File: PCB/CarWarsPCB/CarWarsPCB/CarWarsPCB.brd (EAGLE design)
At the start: 57.1 x 50.5 mm, 11 parts, among them J1 MAGJACK

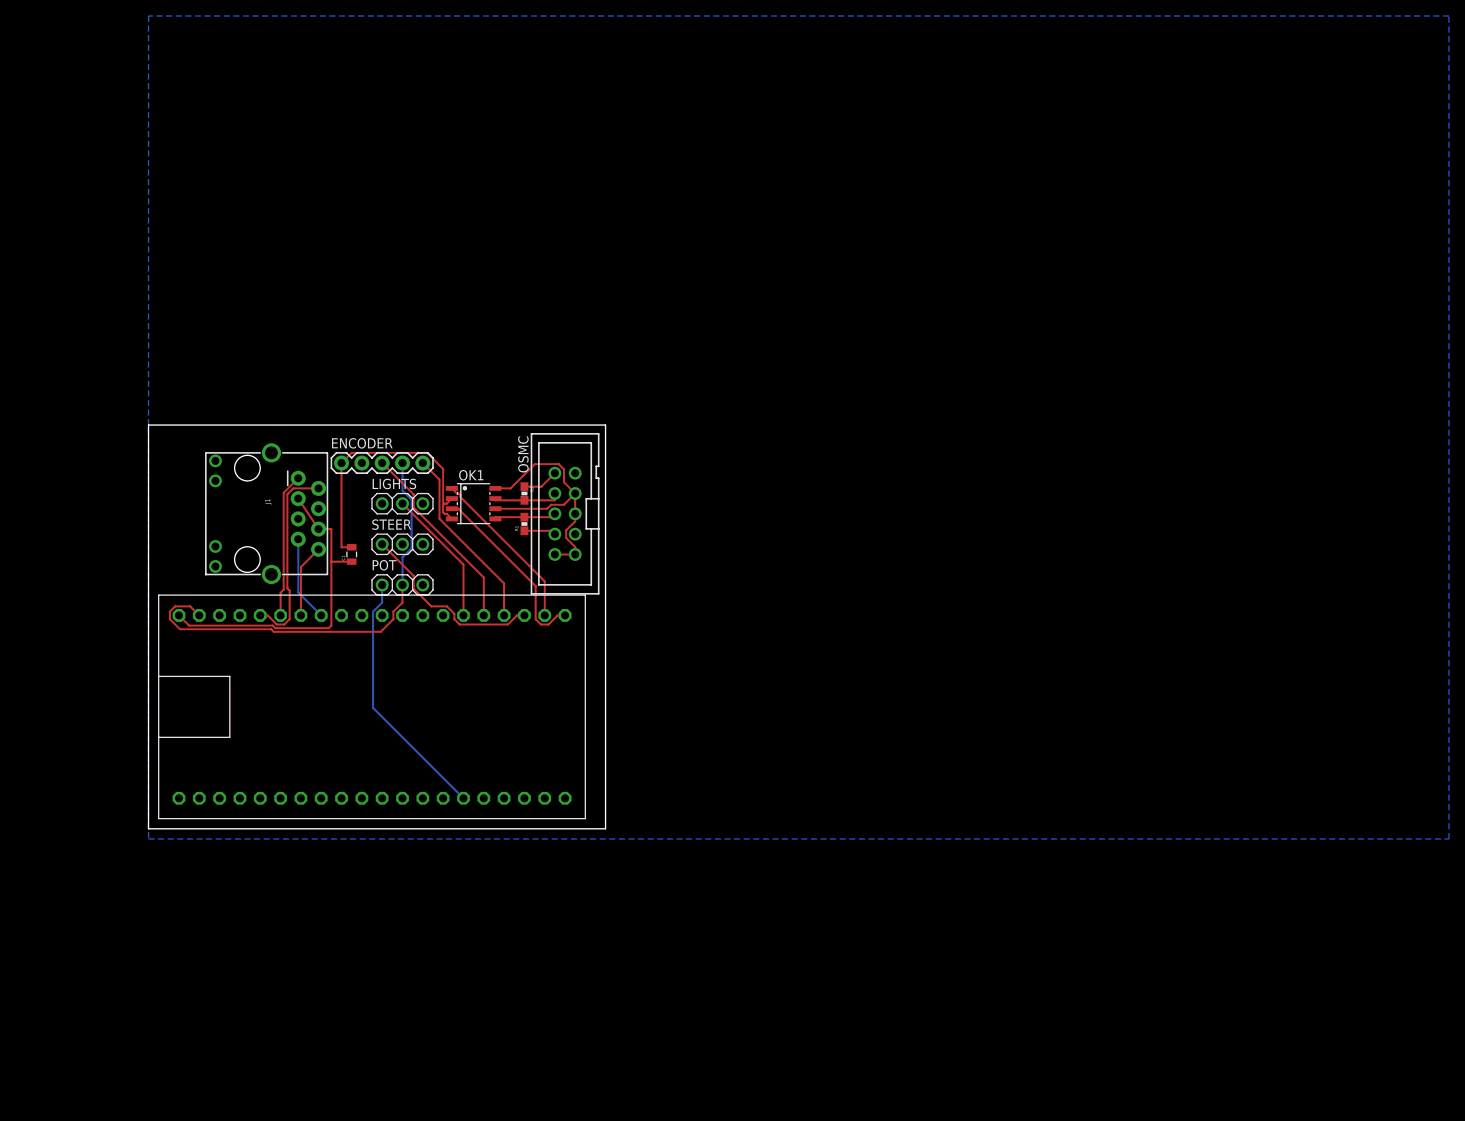
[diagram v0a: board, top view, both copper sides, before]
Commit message: Updated CarWars PCB
Adds barrel jack for power
Re-arranges board
Adds e-stop status connector
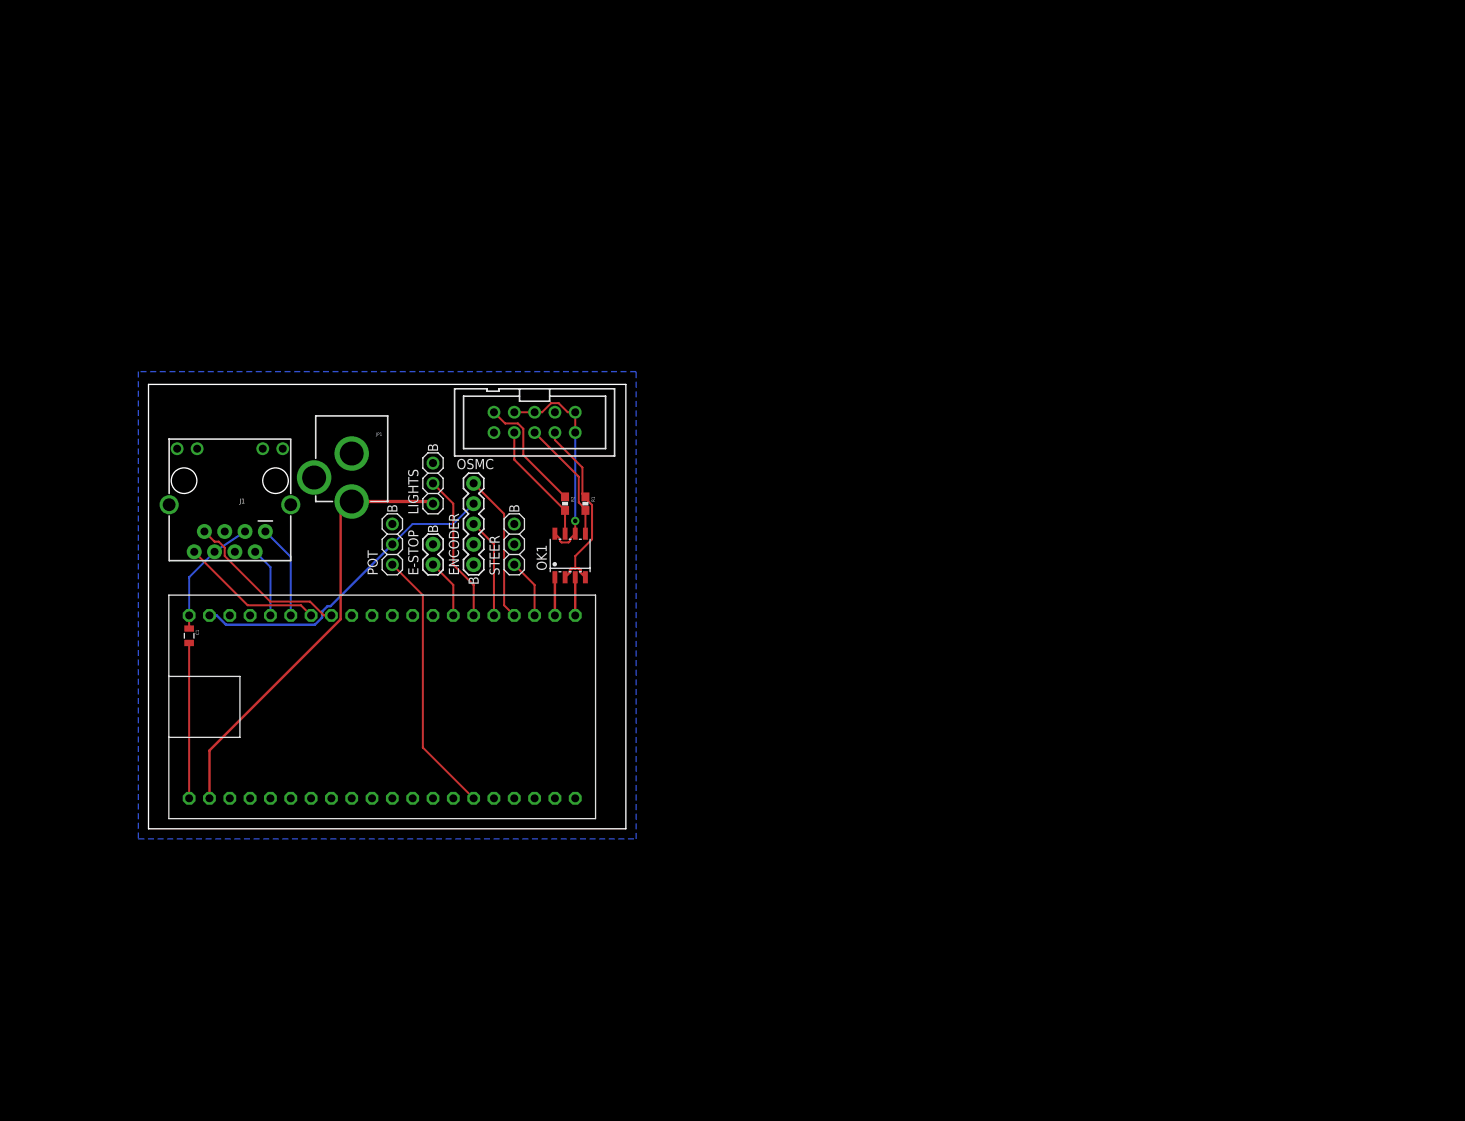
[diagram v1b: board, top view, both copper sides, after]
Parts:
- added E-STOP: (no value), SparkFun-Connectors:1X02
- added JP1: POWER_JACKPTH, SparkFun-Connectors:POWER_JACK_PTH
- moved C1 22.7 mm to (5.08, 24.1), turned to 270 degrees
- moved ENCODER 20.8 mm to (40.6, 33.0), turned to 90 degrees
- moved J1 18.2 mm to (17.8, 54.6), turned to 180 degrees
- moved STEER 14.0 mm to (45.7, 35.6), turned to 90 degrees
- moved OK1 13.7 mm to (52.7, 34.2), turned to 0 degrees
- moved OSMC 12.0 mm to (48.3, 50.8), turned to 180 degrees
- moved R1 8.03 mm to (54.6, 40.6), turned to 270 degrees
- moved POT 5.24 mm to (30.5, 35.6), turned to 90 degrees
- moved R2 5.24 mm to (52.1, 40.6)
- moved LIGHTS 4.58 mm to (35.6, 43.2), turned to 90 degrees
- moved MBED 1.27 mm to (27.9, 15.2)
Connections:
- removed net +24V: OSMC.3
- new net E-STOP_STATUS: E-STOP.1, MBED.27
- new net VCC: JP1.PWR, LIGHTS.1, MBED.2
- net GND: now also E-STOP.2, JP1.GND, JP1.GNDBREAK
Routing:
- net VCC: track 0.00 -> 54.7 mm
- net +3V3: track 40.6 -> 15.5 mm
- net DRIVE_PWM_3V3: track 23.0 -> 4.77 mm
- net STEER_PWM: track 23.7 -> 7.40 mm
- net DRIVE_DIR_3V3: track 20.8 -> 4.77 mm
- net ETH_RD-: track 24.4 -> 8.74 mm
- net +5V: track 55.5 -> 40.2 mm
- net GND: track 42.9 -> 58.2 mm
- net ENC_A: track 24.3 -> 12.5 mm
- net ETH_TD+: track 10.7 -> 20.8 mm
- net ETH_TD-: track 9.17 -> 17.9 mm
- net +12V: track 35.6 -> 27.5 mm, vias 0 -> 1
- net E-STOP_STATUS: track 0.00 -> 7.40 mm
- net DRIVE_PWM_12V: track 8.07 -> 15.3 mm
- net DRIVE_DIR_12V: track 8.50 -> 15.3 mm
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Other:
- board size 57.1 x 50.5 mm -> 59.7 x 55.5 mm
- board text added: "B"

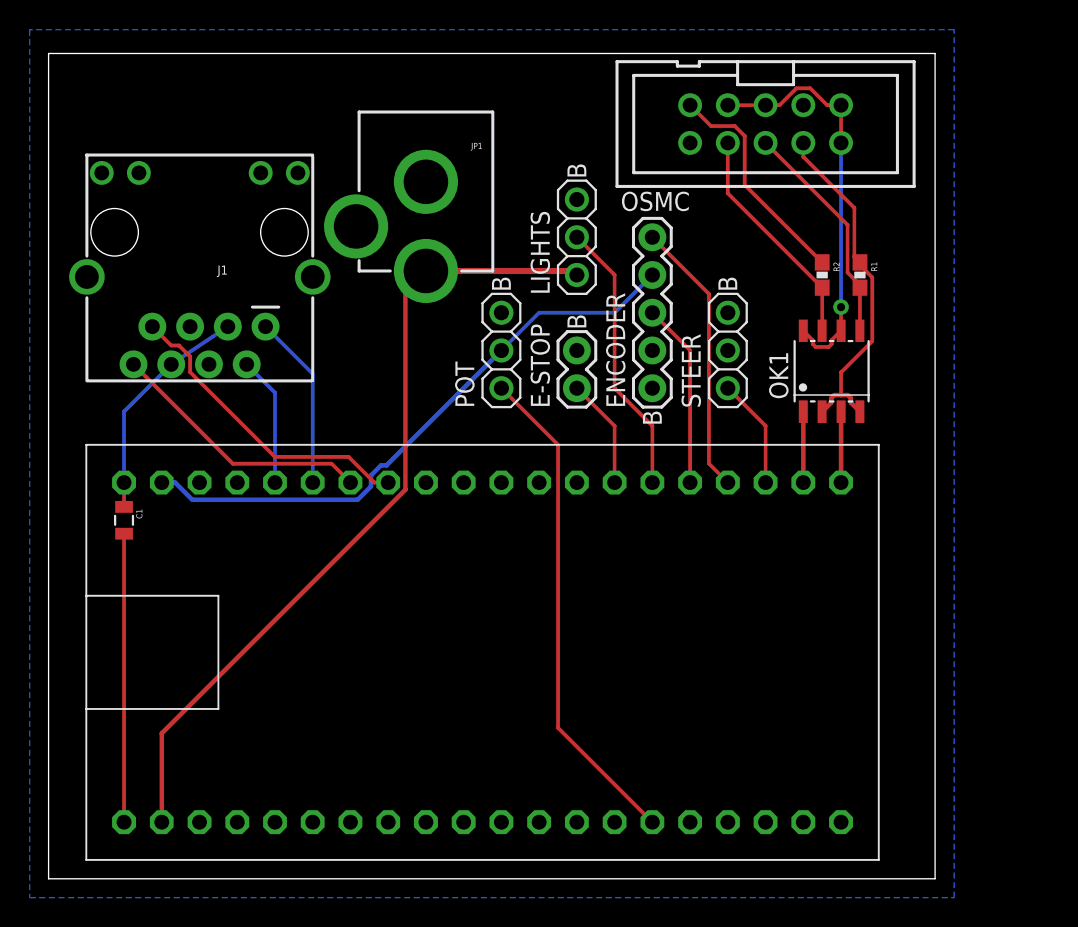
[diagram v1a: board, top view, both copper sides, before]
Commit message: Updates CarWars PCB
Adds connector for SprkFun Current/Voltage sensor
Adds mounting holes to board layout
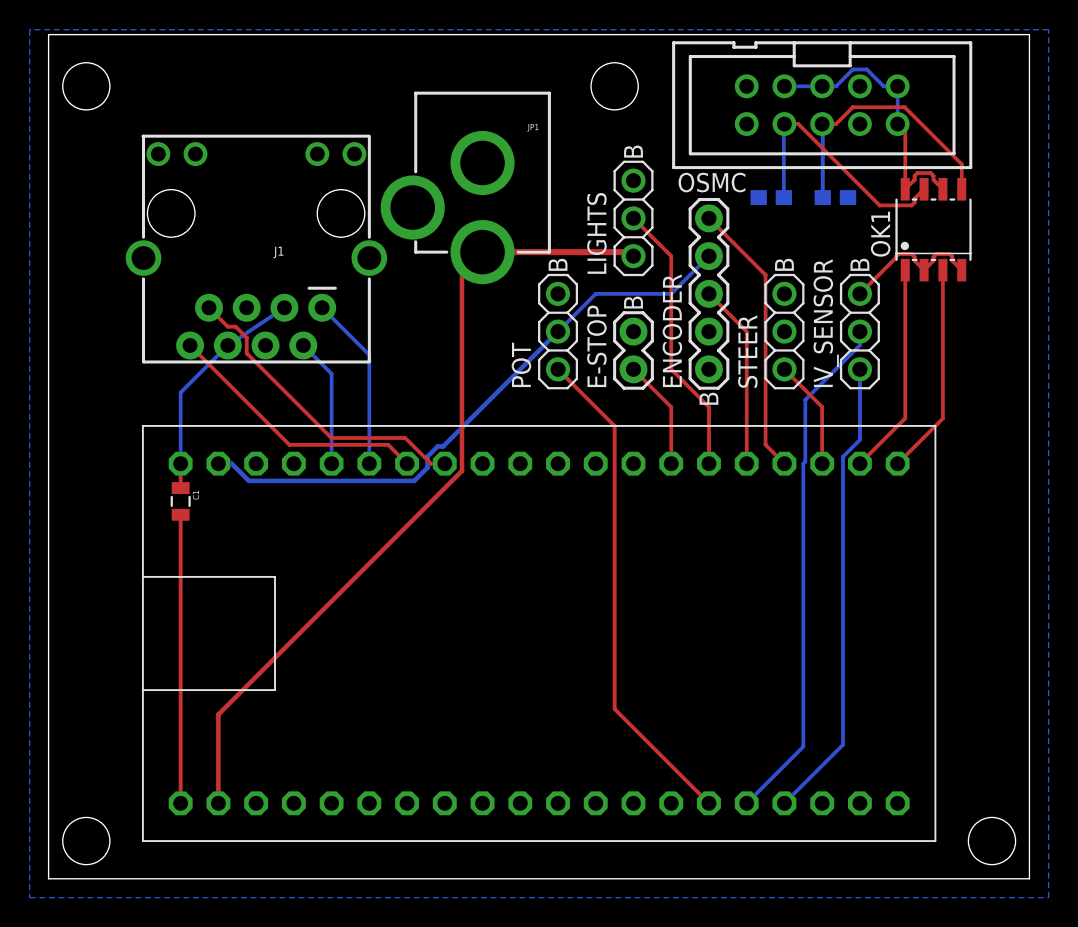
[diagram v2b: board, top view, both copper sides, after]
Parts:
- added IV_SENSOR: (no value), Roboracing:1X03
- moved OK1 11.7 mm to (59.6, 43.7)
- moved R2 6.23 mm to (48.6, 45.8), flipped to the bottom, turned to 180 degrees
- moved R1 5.46 mm to (53.0, 45.8), flipped to the bottom, turned to 0 degrees
- moved JP1 4.02 mm to (29.2, 55.9)
- moved OSMC 4.02 mm to (52.1, 52.1)
- moved ENCODER 4.02 mm to (44.5, 34.3)
- moved STEER 4.02 mm to (49.5, 36.8)
- moved C1 4.02 mm to (8.89, 25.4)
- moved J1 4.02 mm to (21.6, 55.9)
- moved MBED 4.02 mm to (31.8, 16.5)
- moved LIGHTS 4.02 mm to (39.4, 44.5)
- moved POT 4.02 mm to (34.3, 36.8)
- moved E-STOP 4.02 mm to (39.4, 34.3)
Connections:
- new net I_SENSE: IV_SENSOR.1, MBED.17
- new net V_SENSE: IV_SENSOR.2, MBED.16
- net GND: now also IV_SENSOR.3
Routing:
- net V_SENSE: track 0.00 -> 34.9 mm
- net I_SENSE: track 0.00 -> 31.3 mm
- net GND: track 58.2 -> 29.3 mm
- net DRIVE_PWM_3V3: track 4.77 -> 14.3 mm
- net DRIVE_DIR_3V3: track 4.77 -> 14.3 mm
- net +12V: track 27.5 -> 19.4 mm, vias 1 -> 0
- net DRIVE_PWM_12V: track 15.3 -> 18.1 mm
- net DRIVE_DIR_12V: track 15.3 -> 17.2 mm
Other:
- board size 59.7 x 55.5 mm -> 66 x 56.8 mm

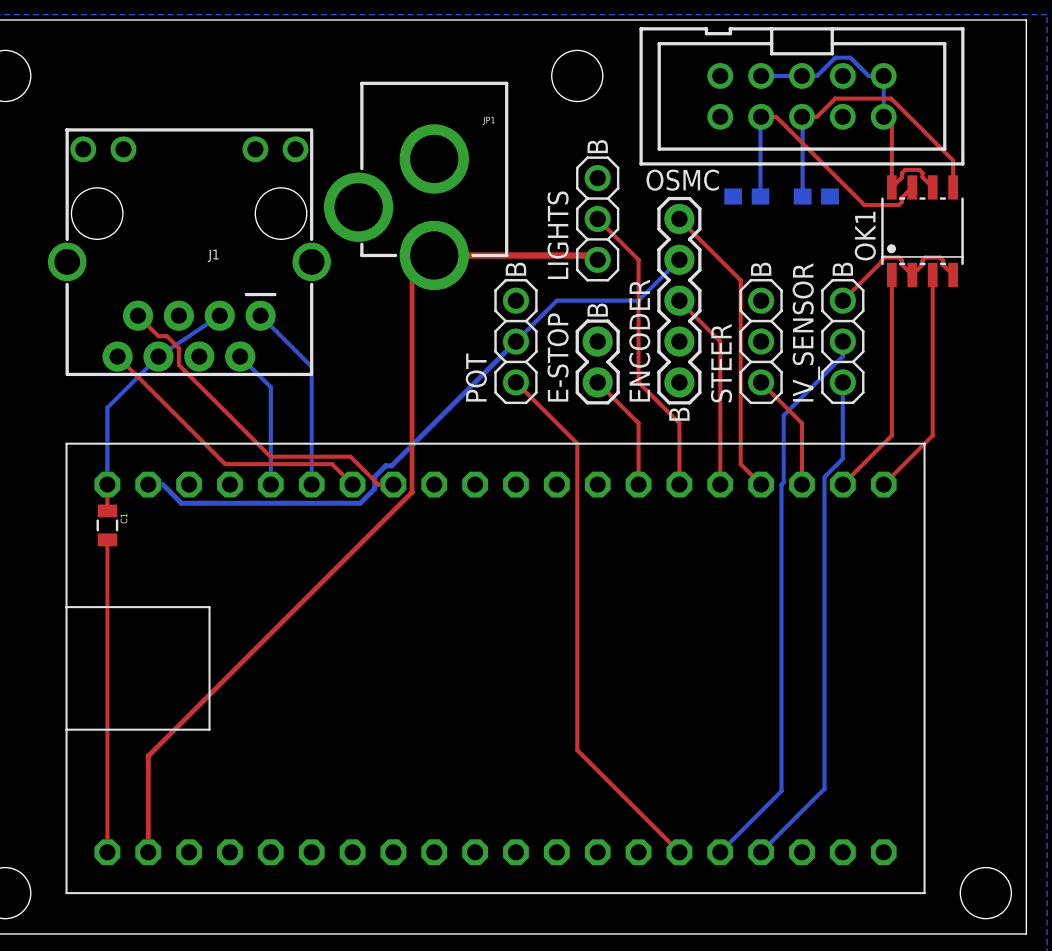
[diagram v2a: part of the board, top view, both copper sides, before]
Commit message: CarWars PCB Prototype finalization
Implements Ryo's recommended changes to OSMC
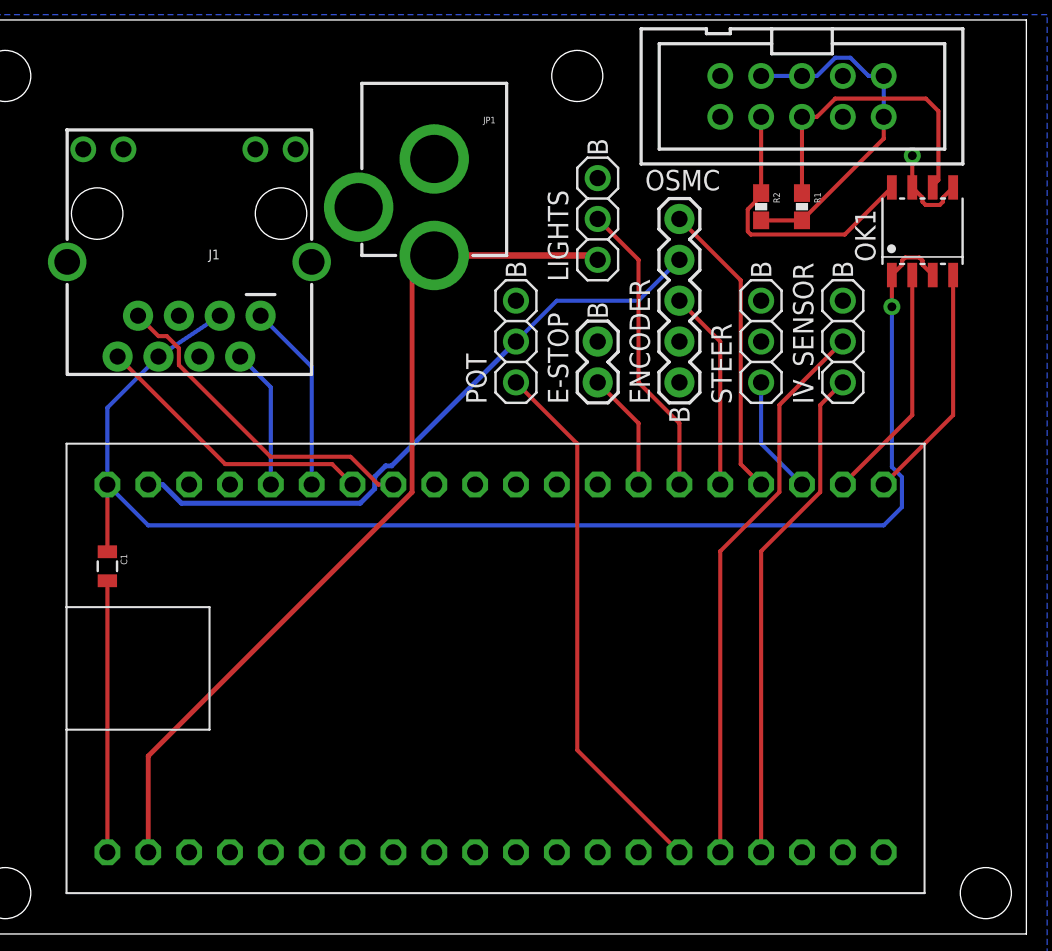
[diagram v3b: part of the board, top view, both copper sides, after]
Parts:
- moved C1 2.54 mm to (8.89, 22.9)
- moved R1 1.09 mm to (52.1, 45.2), flipped to the top, turned to 270 degrees
- moved R2 1.09 mm to (49.5, 45.2), flipped to the top, turned to 270 degrees
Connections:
- net +12V: now also R1.2, R2.2; no longer OK1.6, OK1.8
- net +3V3: now also OK1.1, OK1.3
- net DRIVE_DIR_12V: now also OK1.8, R2.1; no longer OK1.7, R2.2
- net DRIVE_DIR_3V3: now also OK1.2; no longer OK1.1
- net DRIVE_PWM_12V: now also OK1.6, R1.1; no longer OK1.5, R1.2
- net DRIVE_PWM_3V3: now also OK1.4; no longer OK1.3
- net GND: now also OK1.5, OK1.7; no longer OK1.2, OK1.4, R1.1, R2.1
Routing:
- net +3V3: track 15.5 -> 87.4 mm, vias 0 -> 1
- net GND: track 29.3 -> 22.6 mm, vias 0 -> 1
- net +12V: track 19.4 -> 22.2 mm
- net DRIVE_PWM_12V: track 18.1 -> 18.9 mm
- net DRIVE_PWM_3V3: track 14.3 -> 14.8 mm
- net DRIVE_DIR_3V3: track 14.3 -> 14.8 mm
